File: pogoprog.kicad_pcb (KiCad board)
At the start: 4 copper layers, 50 x 20.2 mm, 10 parts, among them J3 Conn_02x06_Odd_Even, M1 Arduino_Mini

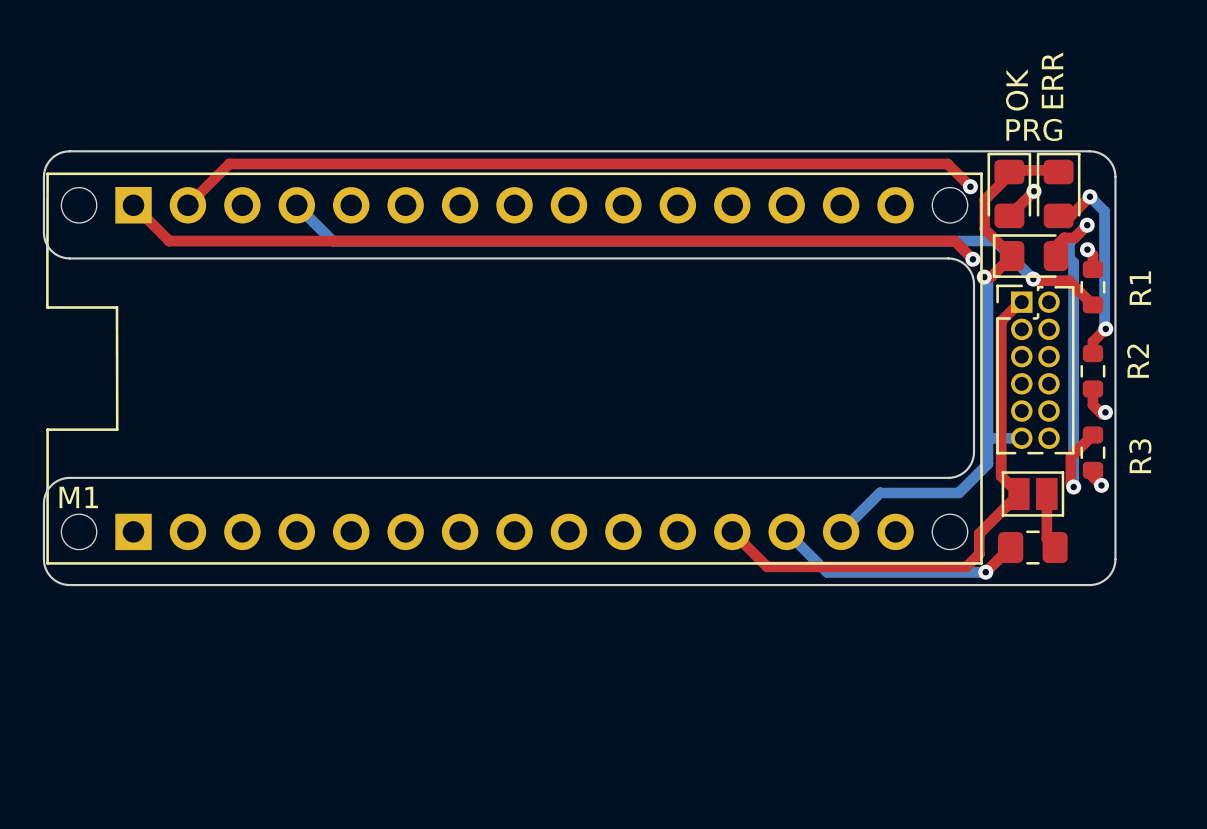
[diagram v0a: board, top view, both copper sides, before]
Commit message: Converted back to 2 layer, as I got the connector size wrong.
Should be 2x6 x 2.54mm pitch
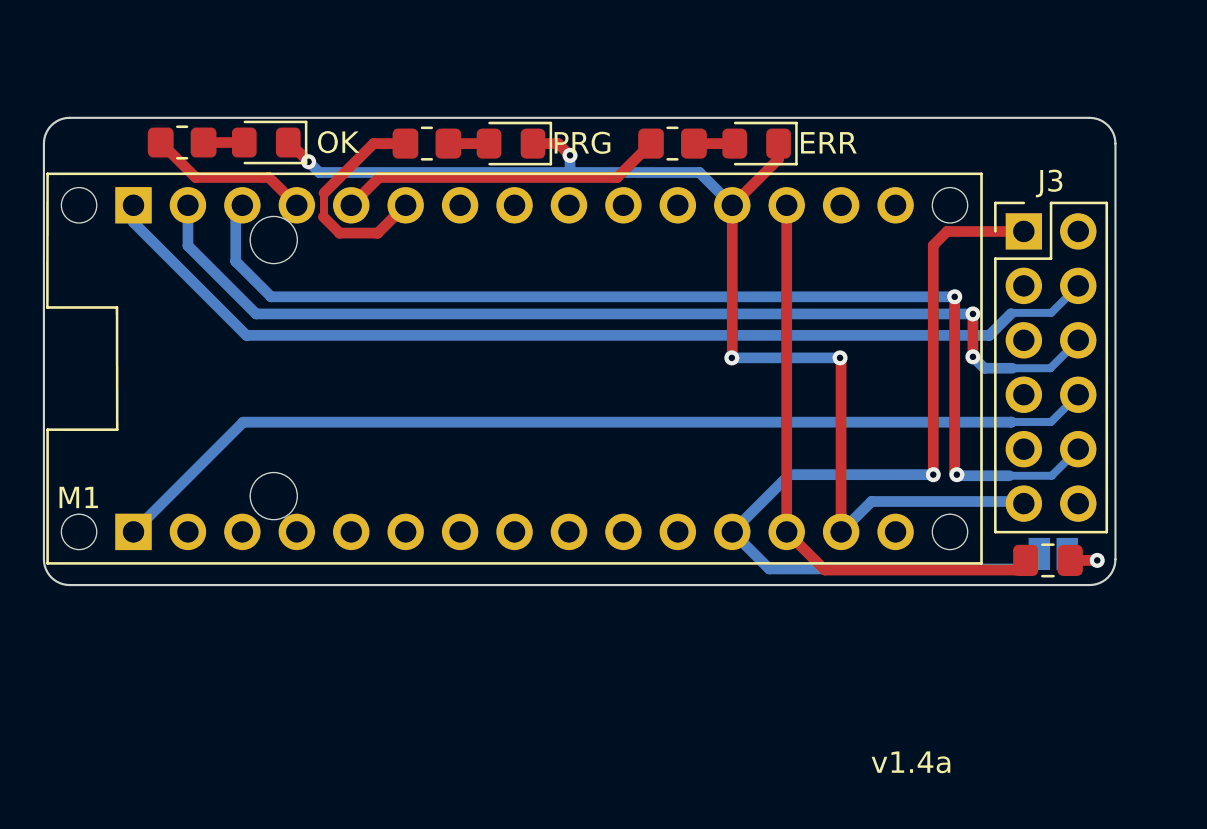
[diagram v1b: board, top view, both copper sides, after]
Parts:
- added H1: MountingHole, MountingHole:MountingHole_2.2mm_M2, F.Cu at (110.3, 85.1)
- added H2: MountingHole, MountingHole:MountingHole_2.2mm_M2, F.Cu at (110.3, 97.0)
- J3: footprint Connector_PinHeader_1.27mm:PinHeader_2x06_P1.27mm_Vertical -> Connector_PinHeader_2.54mm:PinHeader_2x06_P2.54mm_Vertical
- PRG: renamed from JP4; value Jumper_2_Open -> PRG; moved to B.Cu
- R1, R2, R3: footprint Resistor_SMD:R_0603_1608Metric -> Resistor_SMD:R_0805_2012Metric_Pad1.20x1.40mm_HandSolder
- moved R1 43.0 mm to (106.0, 80.5), turned to 0 degrees
- moved D1 34.8 mm to (110.0, 80.5), turned to 180 degrees
- moved R3 34.3 mm to (117.5, 80.6), turned to 0 degrees
- moved D3 25.0 mm to (121.4, 80.6), turned to 180 degrees
- moved R2 22.3 mm to (128.9, 80.6), turned to 0 degrees
- moved D2 14.3 mm to (132.9, 80.6), turned to 180 degrees
- moved J3 3.30 mm to (145.3, 84.7)
- moved PRG 2.96 mm to (146.7, 99.8)
- moved C1 0.92 mm to (146.4, 100.0)
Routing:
- net /D7: track 45.6 -> 10.5 mm, vias 1 -> 0
- net /*D9: track 39.1 -> 7.56 mm, vias 1 -> 0
- net GND: track 27.5 -> 57.9 mm, vias 1 -> 4
- net /D8: track 44.0 -> 15.2 mm, vias 1 -> 0
- net Net-(D3-A): track 17.9 -> 1.90 mm, vias 2 -> 0
- net /~{RESET}: track 11.7 -> 27.3 mm, vias 1 -> 0
- net +5V: track 25.8 -> 41.0 mm, vias 0 -> 1
- net Net-(D2-A): track 9.70 -> 1.90 mm, vias 2 -> 0
- net Net-(D1-A): track 6.42 -> 1.90 mm, vias 2 -> 0
- net /D13/SCK: track 48.7 -> 46.7 mm
- net /*D11/MOSI: track 48.4 -> 47.5 mm, vias 1 -> 2
- net /D12/MISO: track 47.6 -> 48.0 mm, vias 1 -> 0
- net Net-(JP4-B): track 2.66 -> 2.79 mm, vias 0 -> 1
- net /*D10/SS: vias 0 -> 2
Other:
- board size 50 x 20.2 mm -> 50 x 21.8 mm
- copper layers 4 -> 2
- board text added: "mjd 23-May-23"
- board text added: "v1.4a"
- board text removed: "10-May-23"
- board text removed: "mjd v1.3a"
